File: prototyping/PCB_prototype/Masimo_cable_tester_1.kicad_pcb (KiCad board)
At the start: 2 copper layers, 70 x 80 mm, 28 parts, among them J1 Touchscreen HMI, J10 MCU Board Power, J16 Debug Connections, J17 Banana Jack, J2 Curiosity Nano AVR128DB48, J3 Conn_01x28_Socket, J4 Barrel Jack 9V, J5 MicroSD PinHeader, J6 SFML-110-02-L-D-A, J7 HMI Power Toggle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

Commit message: Updated PCB.
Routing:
- net VBUS 5V: track 0.00 -> 24.2 mm
- net Net-(J10-Pin_1): track 0.00 -> 17.6 mm
- net Net-(J3-Pin_27): track 0.00 -> 17.2 mm
- net RSig: track 34.6 -> 40.7 mm
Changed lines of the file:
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@@
+	)
+	(segment
+		(start 121.5 125.385)
+		(end 124.375 125.385)
+		(width 0.2)
+		(layer "F.Cu")
+		(net 4)
 	)
 	(segment
@@
 	)
 	(segment
+		(start 124.375 125.385)
+		(end 126.61 127.62)
+		(width 0.2)
+		(layer "F.Cu")
+		(net 4)
+	)
+	(segment
 		(start 97.76 113.88)
 		(end 111.611 127.731)
@@
 	)
 	(segment
-		(start 124.8064 97)
+		(start 123.6532 98.1532)
+		(end 138.8468 98.1532)
+		(width 0.2)
+		(layer "B.Cu")
+		(net 32)
+	)
+	(segment
+		(start 138.8468 98.1532)
 		(end 140 97)
-		(width 0.2)
-		(layer "B.Cu")
-		(net 32)
-	)
-	(segment
-		(start 123.6532 98.1532)
-		(end 124.8064 97)
 		(width 0.2)
 		(layer "B.Cu")
@@
 	)
 	(segment
+		(start 113 60.54)
+		(end 113 61)
+		(width 0.2)
+		(layer "F.Cu")
+		(net 40)
+	)
+	(segment
+		(start 124.5 72.5)
+		(end 125 72.5)
+		(width 0.2)
+		(layer "F.Cu")
+		(net 40)
+	)
+	(segment
+		(start 113 61)
+		(end 124.5 72.5)
+		(width 0.2)
+		(layer "F.Cu")
+		(net 40)
+	)
+	(segment
 		(start 123.6532 90)
 		(end 123.6532 90.045017)
@@
 	)
 	(segment
-		(start 123.899 95.101)
-		(end 139.101 95.101)
+		(start 123.6532 95.3468)
+		(end 139.3468 95.3468)
 		(width 0.2)
 		(layer "B.Cu")
@@
 	)
 	(segment
-		(start 123.6532 95.3468)
-		(end 123.899 95.101)
+		(start 139.3468 95.3468)
+		(end 140 96)
 		(width 0.2)
 		(layer "B.Cu")
@@
 	)
 	(segment
-		(start 139.101 95.101)
-		(end 140 96)
-		(width 0.2)
-		(layer "B.Cu")
-		(net 49)
+		(start 126.04 76.5)
+		(end 118.8 76.5)
+		(width 0.2)
+		(layer "F.Cu")
+		(net 50)
+	)
+	(segment
+		(start 127.54 78)
+		(end 126.04 76.5)
+		(width 0.2)
+		(layer "F.Cu")
+		(net 50)
+	)
+	(segment
+		(start 113 70.7)
+		(end 118.8 76.5)
+		(width 0.2)
+		(layer "F.Cu")
+		(net 50)
 	)
 	(segment
@@
 	)
 	(segment
-		(start 126 98.5)
+		(start 137.6532 100.8468)
 		(end 140 98.5)
 		(width 0.2)
@@
 	(segment
 		(start 123.6532 100.8468)
-		(end 126 98.5)
+		(end 137.6532 100.8468)
 		(width 0.2)
 		(layer "B.Cu")
@@
 	)
 	(segment
+		(start 91.5 56.5)
+		(end 111.5 56.5)
+		(width 0.2)
+		(layer "F.Cu")
+		(net 53)
+	)
+	(segment
+		(start 90 58)
+		(end 91.5 56.5)
+		(width 0.2)
+		(layer "F.Cu")
+		(net 53)
+	)
+	(segment
+		(start 111.5 56.5)
+		(end 113 58)
+		(width 0.2)
+		(layer "F.Cu")
+		(net 53)
+	)
+	(segment

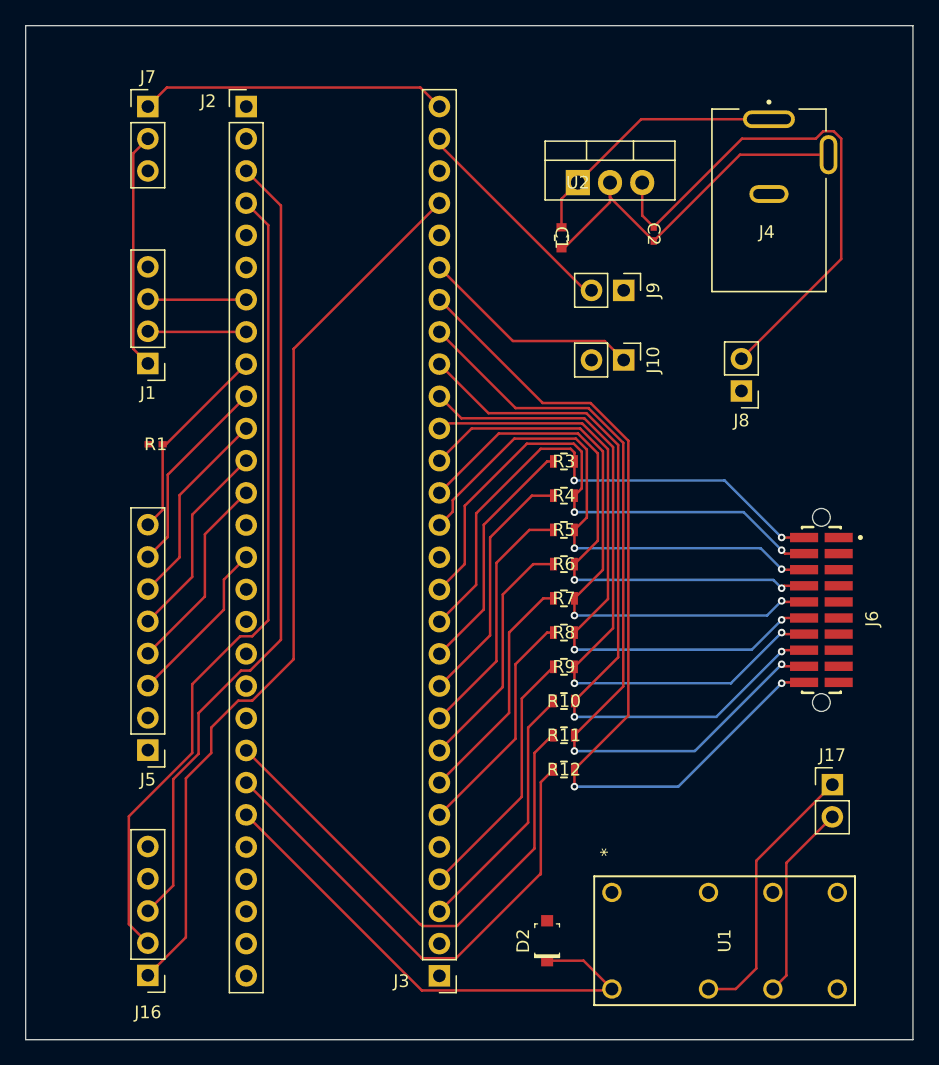
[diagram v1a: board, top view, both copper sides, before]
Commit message: Updated power traces.
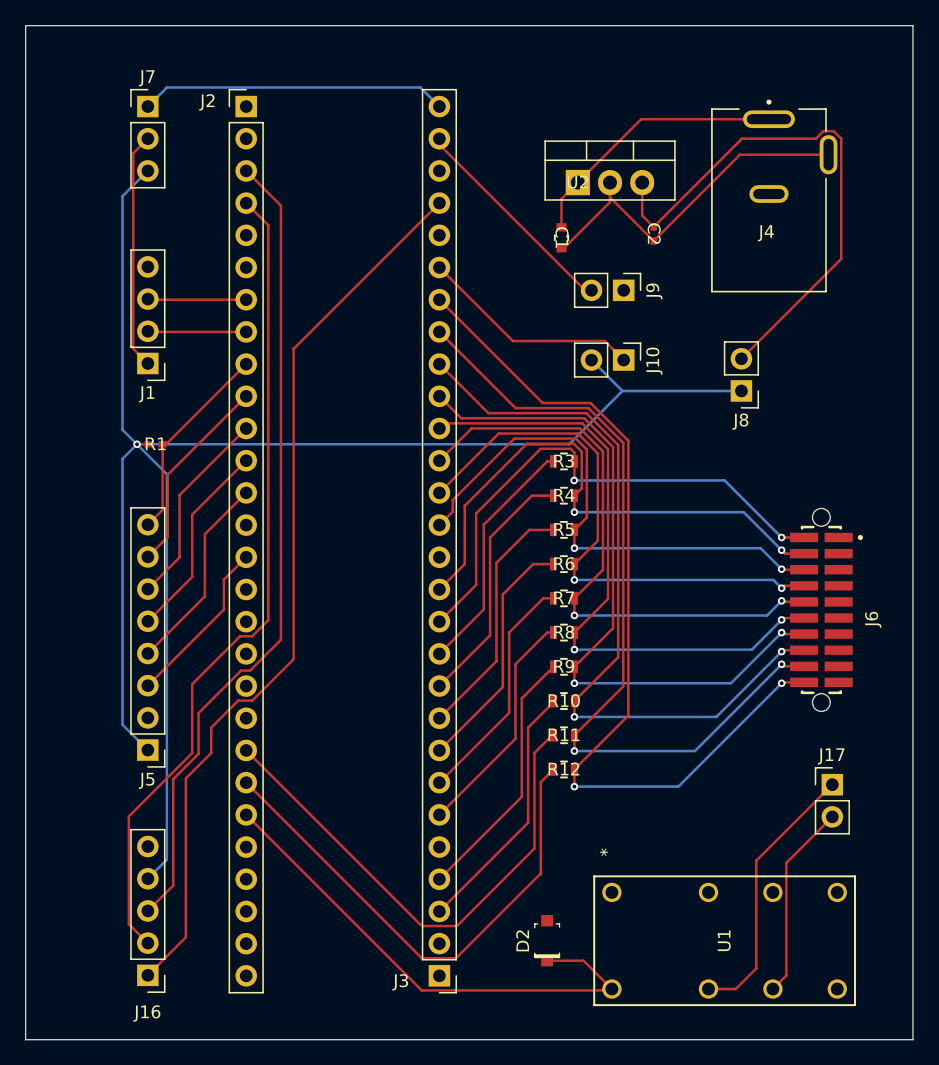
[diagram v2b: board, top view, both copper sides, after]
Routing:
- net 5V: track 0.00 -> 138.0 mm, vias 0 -> 1
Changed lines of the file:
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@@
 		(end 111.5 56.5)
 		(width 0.2)
-		(layer "F.Cu")
+		(layer "B.Cu")
+		(net 53)
+	)
+	(segment
+		(start 111.5 56.5)
+		(end 113 58)
+		(width 0.2)
+		(layer "B.Cu")
 		(net 53)
 	)
@@
 		(end 91.5 56.5)
 		(width 0.2)
-		(layer "F.Cu")
-		(net 53)
-	)
-	(segment
-		(start 111.5 56.5)
-		(end 113 58)
-		(width 0.2)
-		(layer "F.Cu")
+		(layer "B.Cu")
 		(net 53)
 	)
@@
 	)
 	(segment
+		(start 90.061402 84.645)
+		(end 89.145 84.645)
+		(width 0.2)
+		(layer "F.Cu")
+		(net 58)
+	)
+	(via
+		(at 89.145 84.645)
+		(size 0.6)
+		(drill 0.3)
+		(layers "F.Cu" "B.Cu")
+		(net 58)
+	)
+	(segment
+		(start 90 63.08)
+		(end 88 65.08)
+		(width 0.2)
+		(layer "B.Cu")
+		(net 58)
+	)
+	(segment
+		(start 91.5 87)
+		(end 91.5 117.42)
+		(width 0.2)
+		(layer "B.Cu")
+		(net 58)
+	)
+	(segment
+		(start 88 83.5)
+		(end 89.145 84.645)
+		(width 0.2)
+		(layer "B.Cu")
+		(net 58)
+	)
+	(segment
+		(start 136.8278 80.44)
+		(end 127.44 80.44)
+		(width 0.2)
+		(layer "B.Cu")
+		(net 58)
+	)
+	(segment
+		(start 123.235 84.645)
+		(end 127.44 80.44)
+		(width 0.2)
+		(layer "B.Cu")
+		(net 58)
+	)
+	(segment
+		(start 89.145 84.645)
+		(end 91.5 87)
+		(width 0.2)
+		(layer "B.Cu")
+		(net 58)
+	)
+	(segment
+		(start 91.5 117.42)
+		(end 90 118.92)
+		(width 0.2)
+		(layer "B.Cu")
+		(net 58)
+	)
+	(segment
+		(start 89.145 84.645)
+		(end 123.235 84.645)
+		(width 0.2)
+		(layer "B.Cu")
+		(net 58)
+	)
+	(segment
+		(start 90 108.7701)
+		(end 88 106.7701)
+		(width 0.2)
+		(layer "B.Cu")
+		(net 58)
+	)
+	(segment
+		(start 127.44 80.44)
+		(end 125 78)
+		(width 0.2)
+		(layer "B.Cu")
+		(net 58)
+	)
+	(segment
+		(start 88 106.7701)
+		(end 88 85.79)
+		(width 0.2)
+		(layer "B.Cu")
+		(net 58)
+	)
+	(segment
+		(start 88 85.79)
+		(end 89.145 84.645)
+		(width 0.2)
+		(layer "B.Cu")
+		(net 58)
+	)
+	(segment
+		(start 88 65.08)
+		(end 88 83.5)
+		(width 0.2)
+		(layer "B.Cu")
+		(net 58)
+	)
+	(segment

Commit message: Updated Prototype Schematic and PCB
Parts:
- added Q1: 2N3904, Package_TO_SOT_THT:TO-92_Inline, F.Cu at (121.7, 123.9)
- added R2: 1.5kΩ 1/4W, KiCad Symbols and Footprints:RES_ERA8AEB152V, F.Cu at (123.0, 128.5)
- moved D2 12.0 mm to (130.6, 116.0), turned to 180 degrees
- moved J17 1.77 mm to (145.8, 111.5)
- moved U1 1.77 mm to (128.4, 127.6)
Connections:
- net BJ1 renamed Net-(J17-Pin_1)
- net BJ2 renamed Net-(J17-Pin_2)
- net CD renamed Net-(J2-Pin_9)
- net CLK renamed Net-(J2-Pin_13)
- net CS renamed Net-(J2-Pin_10)
- net DI renamed Net-(J2-Pin_11)
- net DO renamed Net-(J2-Pin_12)
- net Rx1 renamed Net-(J1-Pin_3)
- net Rx2 renamed Net-(J16-Pin_3)
- net Tx1 renamed Net-(J1-Pin_2)
- net Tx2 renamed Net-(J16-Pin_2)
- D2 pad A: GND -> Net-(Q1-C)
- D2 pad K: RSig -> 5V
- J2 pad 23: RSig -> Net-(J2-Pin_23)
- U1 pad 1: RSig -> 5V
- U1 pad 8: GND -> Net-(Q1-C)
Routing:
- net RSig: track 40.7 -> 0.00 mm
- net Net-(J2-Pin_23): track 0.00 -> 29.6 mm
- net 5V: track 138.0 -> 151.1 mm
- net Net-(Q1-C): track 0.00 -> 9.97 mm
- net Net-(Q1-B): track 0.00 -> 5.35 mm
